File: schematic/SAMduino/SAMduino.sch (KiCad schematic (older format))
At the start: 0 parts

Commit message: Partial schematic
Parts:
- added C1: 10p, symbol Device:C
- added IC1: ATSAMV71N21B-AABT, QFP50P1600X1600X160-100N, symbol SamacSys_Parts:ATSAMV71N21B-AABT
- added R1: 5k62 +- 1%, symbol Device:R
- added Y?: CM9V-T1A-32.768kHz-12.5pF-20PPM-TA-QC, CM9VT1A, symbol SamacSys_Parts:CM9V-T1A-32.768kHz-12.5pF-20PPM-TA-QC
- added Y?: ASTMUPCE-33-12.000MHZ-LJ-E-T, ASTMUPCE3312000MHZLJET, symbol SamacSys_Parts:ASTMUPCE-33-12.000MHZ-LJ-E-T
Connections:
- new net: C1.1, IC1.97 (VBG), R1.1
- new net CANRX: IC1.20 (PB3)
- new net CANTX: IC1.17 (PB2)
- new net ERASE: IC1.61 (PB12)
- new net GND: C1.2, IC1.10 (GND_4), IC1.29 (GND_5), IC1.3 (GND_1), IC1.6 (VREFN), IC1.67 (GND_6), IC1.7 (GND_2), IC1.8 (GND_3), R1.2
- new net MCLR: IC1.58 (NRST)
- new net Native_D+: IC1.95 (HSDP)
- new net Native_D-: IC1.94 (HSDM)
- new net VCC3V3: IC1.19 (VDDIO_1), IC1.28 (VDDIO_2), IC1.5 (VDDIN), IC1.68 (VDDIO_3), IC1.81 (VDDIO_4), IC1.93 (VDDUTMII)
- new net VDDOUT: IC1.18 (VDDCORE_1), IC1.22 (VDDCORE_2), IC1.39 (VDDCORE_3), IC1.4 (VDDOUT), IC1.76 (VDDCORE_4)
- new net VDDPLL: IC1.86 (VDDPLL)
- new net VDDPLLUSB: IC1.90 (VDDPLLUSB)
- new net VDDUTMIC: IC1.96 (VDDUTMIC)
- new net VREFP: IC1.9 (VREFP)
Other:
- note added: "Flash, CAN and\nUSB to Serial"
- note added: "LEDs, Buttons\nand Headers"
- note added: "Power\nand \nUSB Connectors"

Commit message: Specialty pins wired
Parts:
- removed Y?: CM9V-T1A-32.768kHz-12.5pF-20PPM-TA-QC, CM9VT1A, symbol SamacSys_Parts:CM9V-T1A-32.768kHz-12.5pF-20PPM-TA-QC
- added C? (x2): 22p, symbol Device:C
- added C?: 100n, symbol Device:C
- added Y?: 32.768 kHz, SamacSys_Parts:CM9VT1A, symbol Device:Crystal
- R1: value 5k62 +- 1% -> 5k62 ± 1%
- X?: renamed from Y?; value ASTMUPCE-33-12.000MHZ-LJ-E-T -> 12 MHz
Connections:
- net labels added: HSDM, HSDP, NRST, PB5, QCS, QIO0, QIO1, QIO2, QIO3, QSCK, RXD0, SPI0_MISO, SPI0_MOSI, SPI0_NPCS0, SPI0_SPCK, SWCLK, SWDIO, TWCK0, TWD0, TXD0, URXD0, UTXD0, XIN, XIN32, XOUT32
- net labels removed: MCLR, Native_D+, Native_D-
- wire segments 33 -> 70
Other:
- moved on the sheet: X?

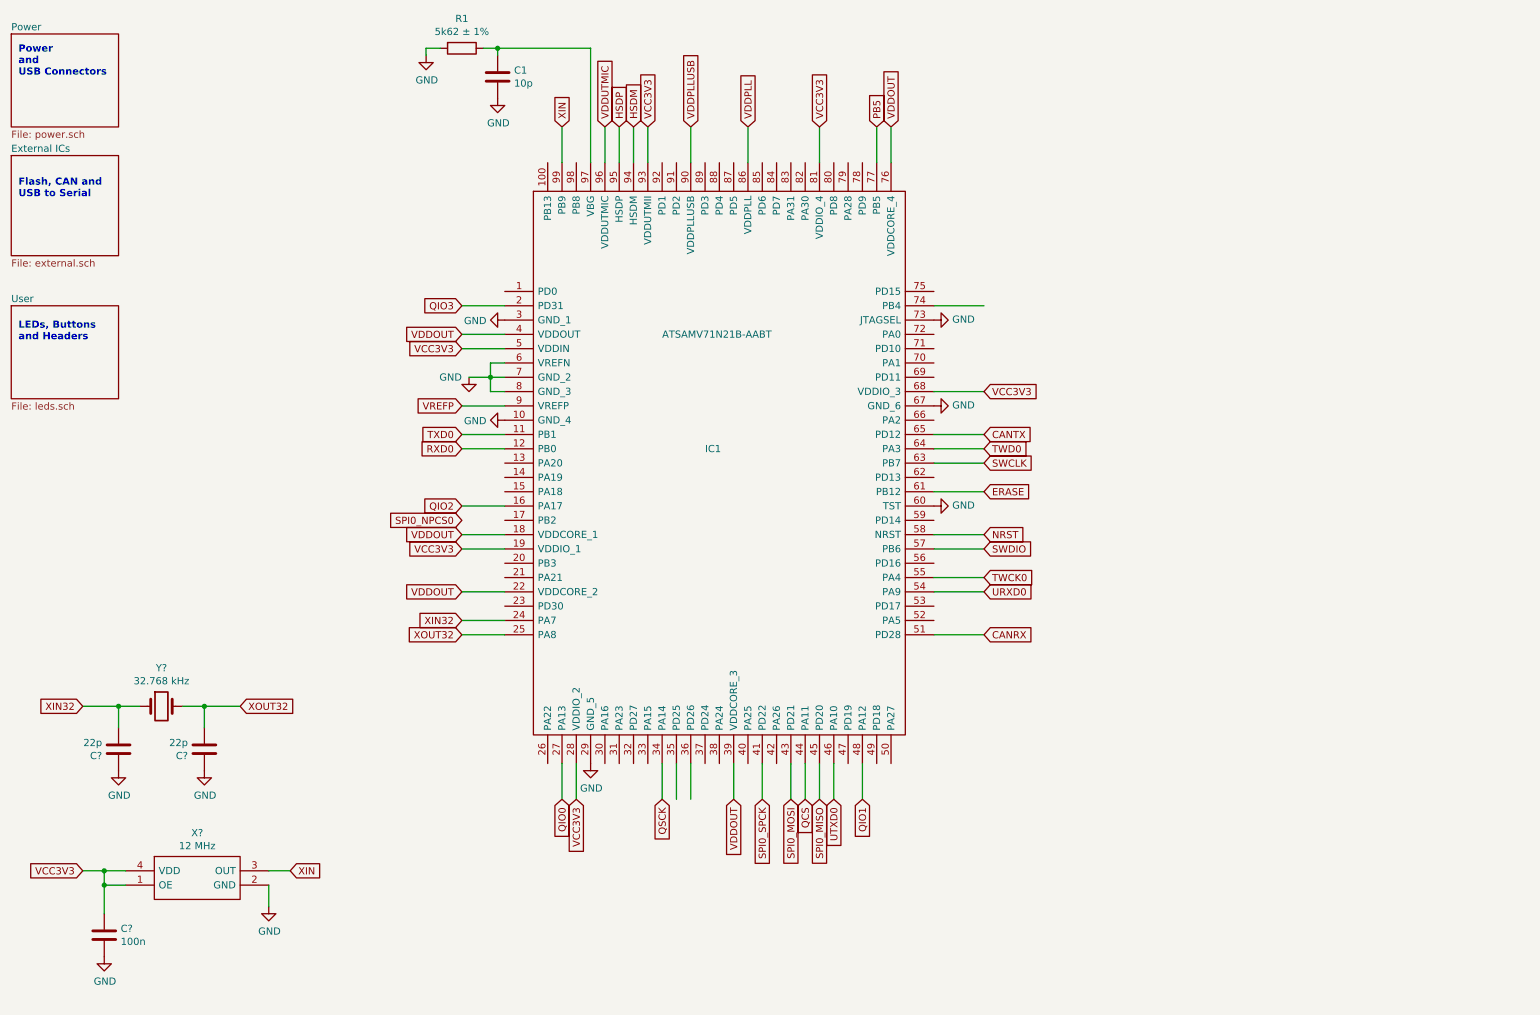
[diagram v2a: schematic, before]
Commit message: All pins connected
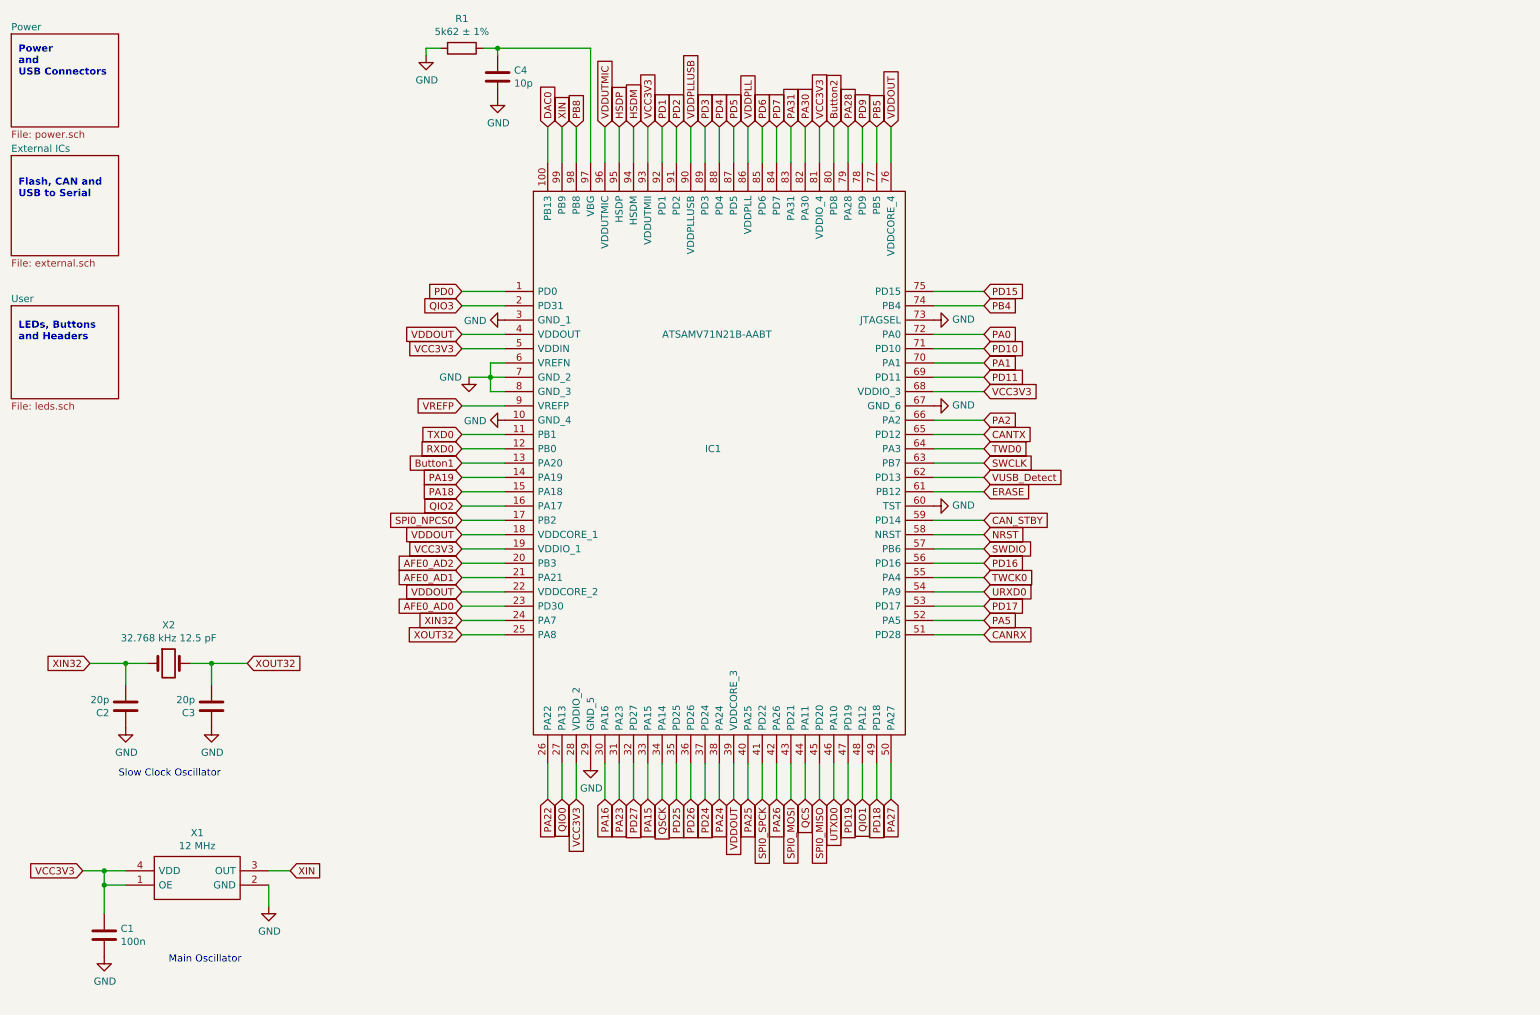
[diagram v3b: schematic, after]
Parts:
- C2, C3: renamed from C?; value 22p -> 20p
- X2: renamed from Y?; value 32.768 kHz -> 32.768 kHz 12.5 pF
- gave numbers to parts that had none: 2
- renumbered C1 to C4
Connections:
- net labels added: AFE0_AD0, AFE0_AD1, AFE0_AD2, Button1, Button2, CAN_STBY, DAC0, PA0, PA1, PA15, PA16, PA18, PA19, PA2, PA22, PA23, PA24, PA25, PA26, PA27, PA28, PA30, PA31, PA5, PB4, PB8, PD0, PD1, PD10, PD11, PD15, PD16, PD17, PD18, PD19, PD2, PD24, PD25, PD26, PD27, PD3, PD4, PD5, PD6, PD7, PD9, VUSB_Detect
- wire segments 70 -> 115
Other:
- note added: "Main Oscillator"
- note added: "Slow Clock Oscillator"
- moved on the sheet: C2, C3, X2

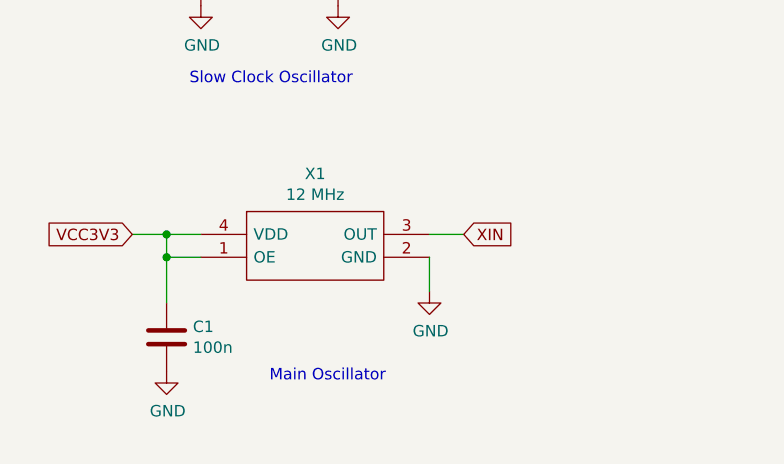
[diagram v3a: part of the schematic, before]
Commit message: Schematic with footprints
Some footprints need to be verified with actual components
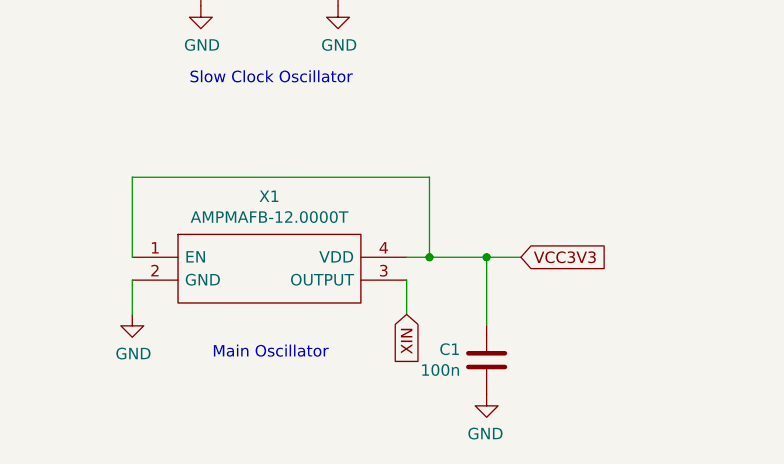
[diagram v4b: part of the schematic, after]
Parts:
- removed X1: 12 MHz, ASTMUPCE3312000MHZLJET, symbol SamacSys_Parts:ASTMUPCE-33-12.000MHZ-LJ-E-T
- added X1: AMPMAFB-12.0000T, SamacSys_Parts:AMPMAFB120000T, symbol SamacSys_Parts:AMPMAFB-12.0000T
- C1: footprint (none) -> Capacitor_SMD:C_0402_1005Metric
- C2, C3, C4: footprint (none) -> Capacitor_SMD:C_0603_1608Metric
- IC1: footprint QFP50P1600X1600X160-100N -> SamacSys_Parts:QFP50P1600X1600X160-100N
- R1: footprint (none) -> Resistor_SMD:R_0402_1005Metric
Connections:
- net GND: now also X1.2 (GND)
- net VCC3V3: now also X1.1 (EN), X1.4 (VDD)
- net XIN: now also X1.3 (OUTPUT)
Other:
- moved on the sheet: C1
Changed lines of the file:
@@
 F 0 "IC1" H 5400 1350 50  0000 L CNN
 F 1 "ATSAMV71N21B-AABT" H 5100 2150 50  0000 L CNN
-F 2 "QFP50P1600X1600X160-100N" H 6850 3150 50  0001 L CNN
+F 2 "SamacSys_Parts:QFP50P1600X1600X160-100N" H 6850 3150 50  0001 L CNN
 F 3 "https://componentsearchengine.com/Datasheets/1/ATSAMV71N21B-AABT.pdf" H 6850 3050 50  0001 L CNN
 F 4 "ARM Microcontrollers - MCU 300Mhz, 2MB Flash, 384KB SRAM, LQFP100, T&R" H 6850 2950 50  0001 L CNN "Description"
@@
 F 0 "R1" V 3493 750 50  0000 C CNN
 F 1 "5k62 ± 1%" V 3584 750 50  0000 C CNN
-F 2 "" V 3630 750 50  0001 C CNN
+F 2 "Resistor_SMD:R_0402_1005Metric" V 3630 750 50  0001 C CNN
 F 3 "~" H 3700 750 50  0001 C CNN
 	1    3700 750
@@
 F 0 "C4" H 4065 996 50  0000 L CNN
 F 1 "10p" H 4065 905 50  0000 L CNN
-F 2 "" H 3988 800 50  0001 C CNN
+F 2 "Capacitor_SMD:C_0603_1608Metric" H 3988 800 50  0001 C CNN
 F 3 "~" H 3950 950 50  0001 C CNN
 	1    3950 950
@@
 	3900 3050 3750 3050
 $Comp
-L SamacSys_Parts:ASTMUPCE-33-12.000MHZ-LJ-E-T X1
-U 1 1 6163D1D7
-P 1350 6500
-F 0 "X1" H 1850 6765 50  0000 C CNN
-F 1 "12 MHz" H 1850 6674 50  0000 C CNN
-F 2 "ASTMUPCE3312000MHZLJET" H 2200 6600 50  0001 L CNN
-F 3 "https://abracon.com/Oscillators/ASTMUPC.pdf" H 2200 6500 50  0001 L CNN
-F 4 "Standard Clock Oscillators MEMS OSC XO 12.0000MHZ LVCMOS" H 2200 6400 50  0001 L CNN "Description"
-F 5 "0.8" H 2200 6300 50  0001 L CNN "Height"
-F 6 "815-UPCE3312LJET" H 2200 6200 50  0001 L CNN "Mouser Part Number"
-F 7 "https://www.mouser.co.uk/ProductDetail/ABRACON/ASTMUPCE-33-12000MHZ-LJ-E-T?qs=%2FPOkb%252BiDxRX9piuXNFIeDg%3D%3D" H 2200 6100 50  0001 L CNN "Mouser Price/Stock"
-F 8 "ABRACON" H 2200 6000 50  0001 L CNN "Manufacturer_Name"
-F 9 "ASTMUPCE-33-12.000MHZ-LJ-E-T" H 2200 5900 50  0001 L CNN "Manufacturer_Part_Number"
-	1    1350 6500
-	1    0    0    -1
-$EndComp
-$Comp
 L Device:C C3
 U 1 1 61634D1C
@@
 F 0 "C3" H 2065 5396 50  0000 L CNN
 F 1 "20p" H 2065 5305 50  0000 L CNN
-F 2 "" H 1988 5200 50  0001 C CNN
+F 2 "Capacitor_SMD:C_0603_1608Metric" H 1988 5200 50  0001 C CNN
 F 3 "~" H 1950 5350 50  0001 C CNN
 	1    1950 5350
@@
 F 0 "C2" H 1465 5396 50  0000 L CNN
 F 1 "20p" H 1465 5305 50  0000 L CNN
-F 2 "" H 1388 5200 50  0001 C CNN
+F 2 "Capacitor_SMD:C_0603_1608Metric" H 1388 5200 50  0001 C CNN
 F 3 "~" H 1350 5350 50  0001 C CNN
 	1    1350 5350
@@
 L Device:C C1
 U 1 1 61635AF8
-P 1200 6950
-F 0 "C1" H 1315 6996 50  0000 L CNN
-F 1 "100n" H 1315 6905 50  0000 L CNN
-F 2 "" H 1238 6800 50  0001 C CNN
-F 3 "~" H 1200 6950 50  0001 C CNN
-	1    1200 6950
-	1    0    0    -1
-$EndComp
-Wire Wire Line
-	1350 6500 1200 6500
-Wire Wire Line
-	1200 6500 1200 6600
-Wire Wire Line
-	1350 6600 1200 6600
-Connection ~ 1200 6600
-Wire Wire Line
-	1200 6600 1200 6800
+P 2600 7050
+F 0 "C1" H 2715 7096 50  0000 L CNN
+F 1 "100n" H 2715 7005 50  0000 L CNN
+F 2 "Capacitor_SMD:C_0402_1005Metric" H 2638 6900 50  0001 C CNN
+F 3 "~" H 2600 7050 50  0001 C CNN
+	1    2600 7050
+	-1   0    0    -1
+$EndComp
 $Comp
 L power:GND #PWR04
 U 1 1 61636FE9
-P 2350 6750
-F 0 "#PWR04" H 2350 6500 50  0001 C CNN
-F 1 "GND" H 2355 6577 50  0000 C CNN
-F 2 "" H 2350 6750 50  0001 C CNN
-F 3 "" H 2350 6750 50  0001 C CNN
-	1    2350 6750
+P 1050 6850
+F 0 "#PWR04" H 1050 6600 50  0001 C CNN
+F 1 "GND" H 1055 6677 50  0000 C CNN
+F 2 "" H 1050 6850 50  0001 C CNN
+F 3 "" H 1050 6850 50  0001 C CNN
+	1    1050 6850
 	1    0    0    -1
 $EndComp
@@
 L power:GND #PWR01
 U 1 1 6163756A
-P 1200 7100
-F 0 "#PWR01" H 1200 6850 50  0001 C CNN
-F 1 "GND" H 1205 6927 50  0000 C CNN
-F 2 "" H 1200 7100 50  0001 C CNN
-F 3 "" H 1200 7100 50  0001 C CNN
-	1    1200 7100
-	1    0    0    -1
-$EndComp
-Wire Wire Line
-	2350 6600 2350 6750
-Text GLabel 1050 6500 0    50   Input ~ 0
+P 2600 7200
+F 0 "#PWR01" H 2600 6950 50  0001 C CNN
+F 1 "GND" H 2605 7027 50  0000 C CNN
+F 2 "" H 2600 7200 50  0001 C CNN
+F 3 "" H 2600 7200 50  0001 C CNN
+	1    2600 7200
+	-1   0    0    -1
+$EndComp
+Wire Wire Line
+	1050 6700 1050 6850
+Text GLabel 2750 6600 2    50   Input ~ 0
 VCC3V3
 Wire Wire Line
-	1050 6500 1200 6500
-Connection ~ 1200 6500
+	2750 6600 2600 6600
+Connection ~ 2600 6600
 $Comp
 L power:GND #PWR02
@@
 Wire Wire Line
 	1950 5050 1950 5200
-Text GLabel 2500 6500 2    50   Input ~ 0
+Text GLabel 2250 6850 3    50   Input ~ 0
 XIN
 Text GLabel 1100 5050 0    50   Input ~ 0
@@
 XOUT32
 Wire Wire Line
-	2350 6500 2500 6500
+	2250 6700 2250 6850
 Wire Wire Line
 	1950 5050 2200 5050
@@
 Wire Wire Line
 	4300 6000 4300 5750
-Text Notes 1650 7150 0    50   ~ 0
+Text Notes 1400 7050 0    50   ~ 0
 Main Oscillator
 Text Notes 1300 5850 0    50   ~ 0
 Slow Clock Oscillator
+$Comp
+L SamacSys_Parts:AMPMAFB-12.0000T X1
+U 1 1 6171D4C5
+P 1050 6600
+F 0 "X1" H 1650 6865 50  0000 C CNN
+F 1 "AMPMAFB-12.0000T" H 1650 6774 50  0000 C CNN
+F 2 "SamacSys_Parts:AMPMAFB120000T" H 2100 6700 50  0001 L CNN
+F 3 "https://datasheet.datasheetarchive.com/originals/dk/DKDS41/DSANUWW0031017.pdf" H 2100 6600 50  0001 L CNN
+F 4 "Standard Clock Oscillators MEMS OSC XO 12.0000MHZ SMD" H 2100 6500 50  0001 L CNN "Description"
+F 5 "0.89" H 2100 6400 50  0001 L CNN "Height"
+F 6 "815-AMPMAFB-12.0000T" H 2100 6300 50  0001 L CNN "Mouser Part Number"
+F 7 "https://www.mouser.co.uk/ProductDetail/ABRACON/AMPMAFB-120000T?qs=%252BEew9%252B0nqrB9Y5kN3McktA%3D%3D" H 2100 6200 50  0001 L CNN "Mouser Price/Stock"
+F 8 "ABRACON" H 2100 6100 50  0001 L CNN "Manufacturer_Name"
+F 9 "AMPMAFB-12.0000T" H 2100 6000 50  0001 L CNN "Manufacturer_Part_Number"
+	1    1050 6600
+	1    0    0    -1
+$EndComp
+Wire Wire Line
+	2600 6600 2600 6900
+Wire Wire Line
+	2250 6600 2350 6600
+Wire Wire Line
+	2350 6600 2350 6250
+Wire Wire Line
+	2350 6250 1050 6250
+Wire Wire Line
+	1050 6250 1050 6600
+Connection ~ 2350 6600
+Wire Wire Line
+	2350 6600 2600 6600
 $EndSCHEMATC

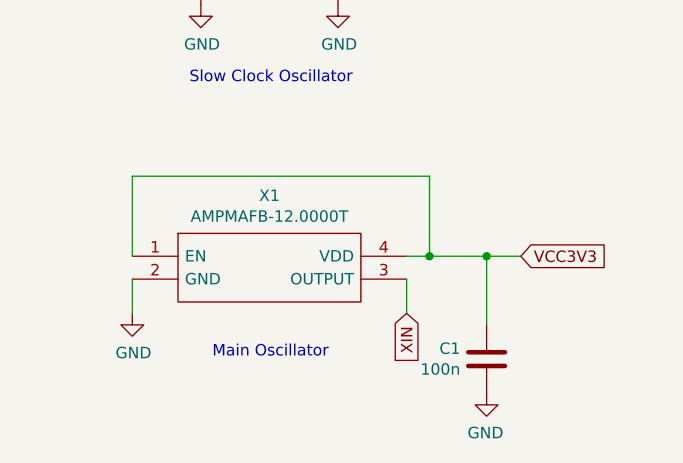
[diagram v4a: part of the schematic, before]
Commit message: Changed oscillator to 3.2x2.5 size
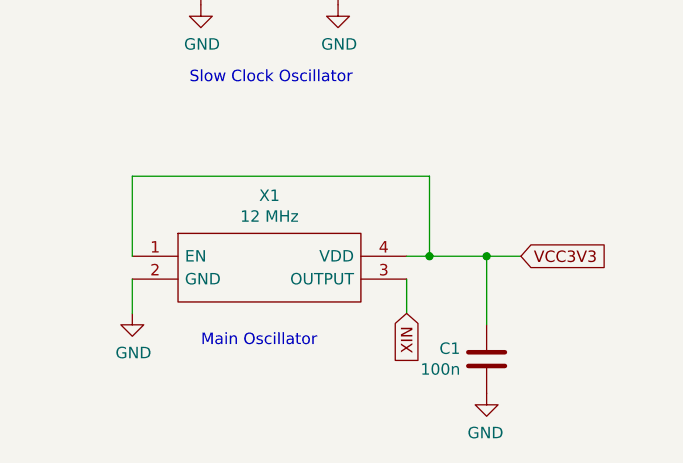
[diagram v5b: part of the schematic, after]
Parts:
- X1: value AMPMAFB-12.0000T -> 12 MHz; footprint SamacSys_Parts:AMPMAFB120000T -> SamacSys_Parts:ASTMUPCE3312000MHZLJET; Description Standard Clock Oscillators MEMS OSC XO 12.0000MHZ SMD -> 12 MHz Crystal or MEMS oscillator; Manufacturer_Name ABRACON -> (none); Manufacturer_Part_Number AMPMAFB-12.0000T -> (none); Mouser Part Number 815-AMPMAFB-12.0000T -> (none); Mouser Price/Stock https://www.mouser.co.uk/ProductDetail/ABRACON/AMPMAFB-1200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 -> (none)
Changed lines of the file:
@@
 Wire Wire Line
 	4300 6000 4300 5750
-Text Notes 1400 7050 0    50   ~ 0
+Text Notes 1350 7000 0    50   ~ 0
 Main Oscillator
 Text Notes 1300 5850 0    50   ~ 0
@@
 P 1050 6600
 F 0 "X1" H 1650 6865 50  0000 C CNN
-F 1 "AMPMAFB-12.0000T" H 1650 6774 50  0000 C CNN
-F 2 "SamacSys_Parts:AMPMAFB120000T" H 2100 6700 50  0001 L CNN
-F 3 "https://datasheet.datasheetarchive.com/originals/dk/DKDS41/DSANUWW0031017.pdf" H 2100 6600 50  0001 L CNN
-F 4 "Standard Clock Oscillators MEMS OSC XO 12.0000MHZ SMD" H 2100 6500 50  0001 L CNN "Description"
+F 1 "12 MHz" H 1650 6774 50  0000 C CNN
+F 2 "SamacSys_Parts:ASTMUPCE3312000MHZLJET" H 2100 6700 50  0001 L CNN
+F 3 "" H 2100 6600 50  0001 L CNN
+F 4 "12 MHz Crystal or MEMS oscillator" H 2100 6500 50  0001 L CNN "Description"
 F 5 "0.89" H 2100 6400 50  0001 L CNN "Height"
-F 6 "815-AMPMAFB-12.0000T" H 2100 6300 50  0001 L CNN "Mouser Part Number"
-F 7 "https://www.mouser.co.uk/ProductDetail/ABRACON/AMPMAFB-120000T?qs=%252BEew9%252B0nqrB9Y5kN3McktA%3D%3D" H 2100 6200 50  0001 L CNN "Mouser Price/Stock"
-F 8 "ABRACON" H 2100 6100 50  0001 L CNN "Manufacturer_Name"
-F 9 "AMPMAFB-12.0000T" H 2100 6000 50  0001 L CNN "Manufacturer_Part_Number"
+F 6 "" H 2100 6300 50  0001 L CNN "Mouser Part Number"
+F 7 "" H 2100 6200 50  0001 L CNN "Mouser Price/Stock"
+F 8 "" H 2100 6100 50  0001 L CNN "Manufacturer_Name"
+F 9 "" H 2100 6000 50  0001 L CNN "Manufacturer_Part_Number"
 	1    1050 6600
 	1    0    0    -1
